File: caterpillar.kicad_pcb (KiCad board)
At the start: 2 copper layers, 20.2 x 20.2 mm, 34 parts, among them J1 Conn_ARM_JTAG_SWD_10, M1 Conn_01x02_Pin, M2 *, M3 Conn_01x02_Pin, U1 STBB1-APUR, U2 ASM330LHHTR, U3 DRV8212P, U4 ADP2503ACPZ-3.3-R7, U6 max5419leta+T

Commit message: logos: extract kamoamoa into library; drop previous designer's mark
- Extract the kamoamoa back-silkscreen logo from the board into
  library/Logos/footprints.pretty/ and register nickname "Logos",
  resolving the dangling Logos:kamoamoa reference
- Remove the Kicad_library:Personal_small footprint (39-polygon
  personal mark of the original designer; its source library never
  existed on this machine)
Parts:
- removed the G*** at (113.5, 93.0)

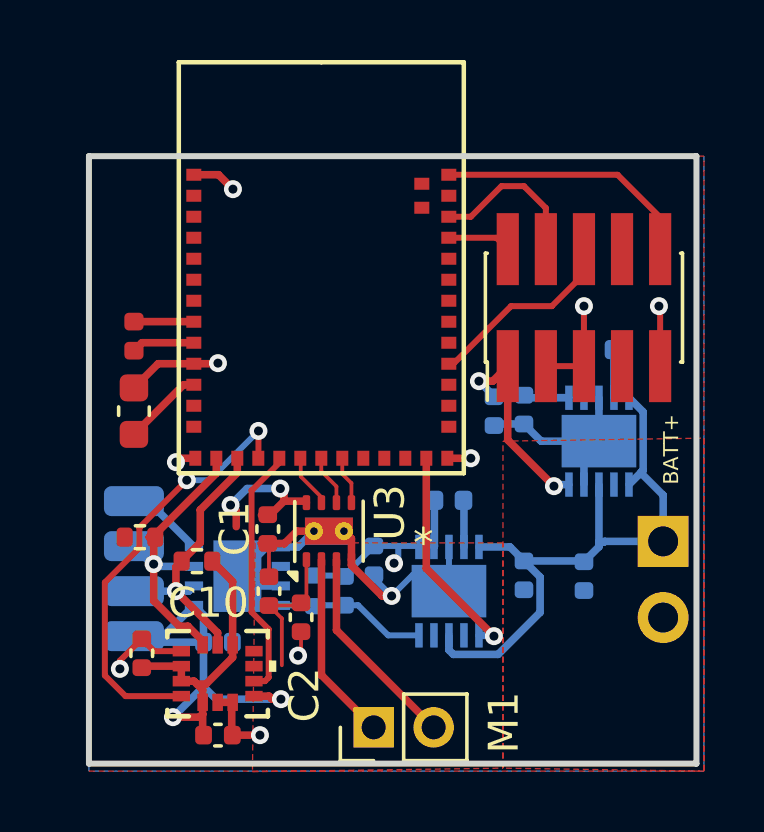
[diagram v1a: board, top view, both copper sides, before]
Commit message: library: add Castellated_2PTH_P1.27mm joined dual-hole solder point
Two 2.54mm-header-style PTH (1.7mm pad, 1.0mm drill) at 1.27mm pitch,
bridged by copper rect pads on front and back between the pad
outlines; all pads share number 1. Single-pin symbol, excluded from
BOM/position files. Note: 0.27mm drill-to-drill web -- confirm with fab.
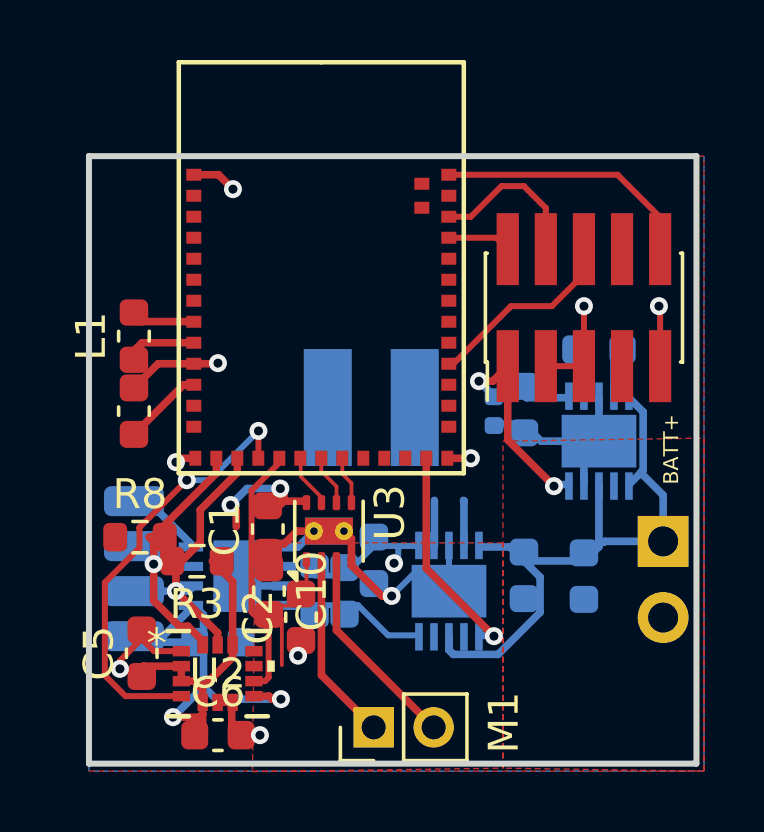
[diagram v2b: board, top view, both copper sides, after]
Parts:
- C1, C10, C11, C12, C2, C3, C5, C6, C7, C8, C9: footprint Capacitor_SMD:C_0402_1005Metric -> Capacitor_SMD:C_0603_1608Metric
- L1, L6: footprint Inductor_SMD:L_0402_1005Metric -> Inductor_SMD:L_0603_1608Metric
- L5: footprint Inductor_SMD:L_0402_1005Metric -> VLCF4020T-2R2N1R7:VLCF4020
- R3, R4, R8: footprint Resistor_SMD:R_0402_1005Metric -> Resistor_SMD:R_0603_1608Metric
- U1: footprint STBB1_APUR:SON_B1-APUR_STM -> STBB1_APUR:SON_B1-APUR_STM-M
- U2: footprint ASM330LHHTR:LGA-14L_2P5X3X0P83_STM -> ASM330LHHTR:LGA-14L_2P5X3X0P83_STM-L
- U4: footprint ADP2503ACPZ_3_3_R7:CP_10_9_ADI -> ADP2503ACPZ_3_3_R7:CP_10_9_ADI-M
- U6: footprint max5419:21-0137_T833&plus_2_MXM-L -> max5419:21-0137_T833&plus_2_MXM-M
- moved L5 4.03 mm to (117.4, 98.4)

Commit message: pcb: remove orphaned duplicate C8 (4.7uF 0402)
A manually-placed 3.3V decoupling cap with no schematic symbol shared
the C8 reference with the real 22uF cap. No tool flagged it: pcbnew
does not enforce unique references, F8 does not delete unmatched
footprints by default, and DRC schematic-parity is opt-in.
Note: already-fabricated boards do have this cap fitted.
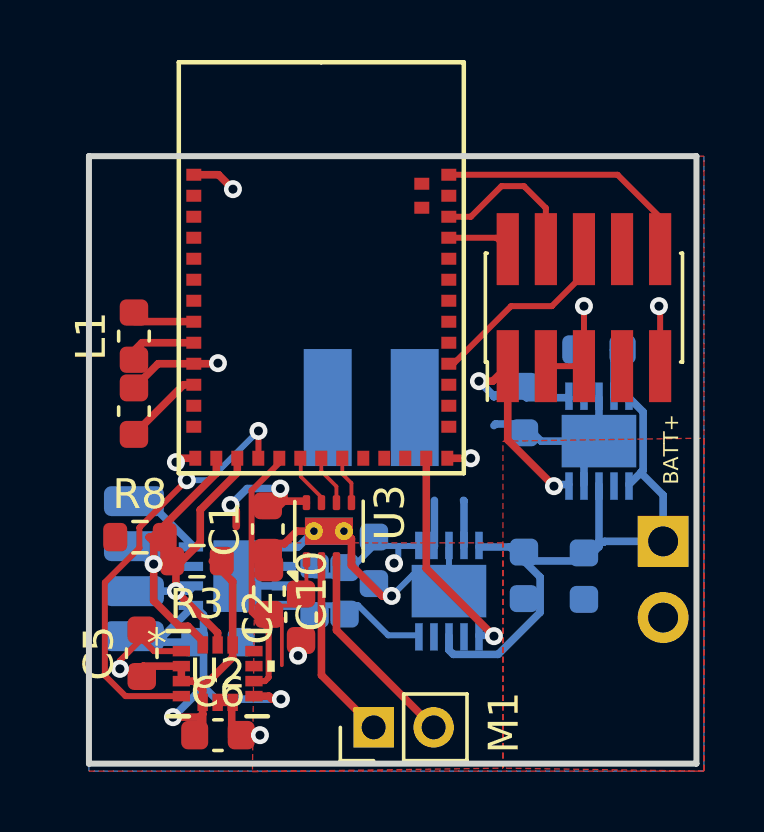
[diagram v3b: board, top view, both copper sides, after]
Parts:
- removed the C8 at (121.5, 98.5)
